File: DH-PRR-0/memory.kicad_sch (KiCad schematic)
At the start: 7 parts, among them J2 Micro_SD_Card_Det2, J3 USB3_A

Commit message: alternate power topologies
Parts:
- renumbered R16 to R30, R17 to R31, R18 to R32, R19 to R33, R20 to R34
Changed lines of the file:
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@@
 		(dnp no)
 		(fields_autoplaced yes)
-		(property "Reference" "#PWR034"
+		(property "Reference" "#PWR056"
 			(at 152.4 107.95 0)
 			(hide yes)
@@
 			(project "DH-PRR-0"
 				(path "/ef4cbb1a-0736-46e9-bda5-652f30ffa2fe/64c9e3bf-941e-41e6-9266-e7d08c7e7040"
-					(reference "#PWR034")
+					(reference "#PWR056")
 					(unit 1)
 				)
@@
 		(dnp no)
 		(fields_autoplaced yes)
-		(property "Reference" "#PWR033"
+		(property "Reference" "#PWR057"
 			(at 165.1 154.94 0)
 			(hide yes)
@@
 			(project "DH-PRR-0"
 				(path "/ef4cbb1a-0736-46e9-bda5-652f30ffa2fe/64c9e3bf-941e-41e6-9266-e7d08c7e7040"
-					(reference "#PWR033")
+					(reference "#PWR057")
 					(unit 1)
 				)
@@
 		(in_pos_files yes)
 		(dnp no)
-		(property "Reference" "R19"
+		(property "Reference" "R33"
 			(at 163.83 113.03 90)
 			(show_name no)
@@
 			(project "DH-PRR-0"
 				(path "/ef4cbb1a-0736-46e9-bda5-652f30ffa2fe/64c9e3bf-941e-41e6-9266-e7d08c7e7040"
-					(reference "R19")
+					(reference "R33")
 					(unit 1)
 				)
@@
 		(dnp no)
 		(fields_autoplaced yes)
-		(property "Reference" "#PWR036"
+		(property "Reference" "#PWR060"
 			(at 248.92 154.94 0)
 			(hide yes)
@@
 			(project "DH-PRR-0"
 				(path "/ef4cbb1a-0736-46e9-bda5-652f30ffa2fe/64c9e3bf-941e-41e6-9266-e7d08c7e7040"
-					(reference "#PWR036")
+					(reference "#PWR060")
 					(unit 1)
 				)
@@
 		(dnp no)
 		(fields_autoplaced yes)
-		(property "Reference" "#PWR032"
+		(property "Reference" "#PWR059"
 			(at 210.82 154.94 0)
 			(hide yes)
@@
 			(project "DH-PRR-0"
 				(path "/ef4cbb1a-0736-46e9-bda5-652f30ffa2fe/64c9e3bf-941e-41e6-9266-e7d08c7e7040"
-					(reference "#PWR032")
+					(reference "#PWR059")
 					(unit 1)
 				)
@@
 		(in_pos_files yes)
 		(dnp no)
-		(property "Reference" "R20"
+		(property "Reference" "R34"
 			(at 166.37 113.03 90)
 			(show_name no)
@@
 			(project "DH-PRR-0"
 				(path "/ef4cbb1a-0736-46e9-bda5-652f30ffa2fe/64c9e3bf-941e-41e6-9266-e7d08c7e7040"
-					(reference "R20")
+					(reference "R34")
 					(unit 1)
 				)
@@
 		(in_pos_files yes)
 		(dnp no)
-		(property "Reference" "R18"
+		(property "Reference" "R32"
 			(at 161.29 113.03 90)
 			(show_name no)
@@
 			(project "DH-PRR-0"
 				(path "/ef4cbb1a-0736-46e9-bda5-652f30ffa2fe/64c9e3bf-941e-41e6-9266-e7d08c7e7040"
-					(reference "R18")
+					(reference "R32")
 					(unit 1)
 				)
@@
 		(in_pos_files yes)
 		(dnp no)
-		(property "Reference" "R17"
+		(property "Reference" "R31"
 			(at 158.75 113.03 90)
 			(show_name no)
@@
 			(project "DH-PRR-0"
 				(path "/ef4cbb1a-0736-46e9-bda5-652f30ffa2fe/64c9e3bf-941e-41e6-9266-e7d08c7e7040"
-					(reference "R17")
+					(reference "R31")
 					(unit 1)
 				)
@@
 		(in_pos_files yes)
 		(dnp no)
-		(property "Reference" "R16"
+		(property "Reference" "R30"
 			(at 156.21 113.03 90)
 			(show_name no)
@@
 			(project "DH-PRR-0"
 				(path "/ef4cbb1a-0736-46e9-bda5-652f30ffa2fe/64c9e3bf-941e-41e6-9266-e7d08c7e7040"
-					(reference "R16")
+					(reference "R30")
 					(unit 1)
 				)
@@
 		(dnp no)
 		(fields_autoplaced yes)
-		(property "Reference" "#PWR035"
+		(property "Reference" "#PWR058"
 			(at 177.8 154.94 0)
 			(hide yes)
@@
 			(project "DH-PRR-0"
 				(path "/ef4cbb1a-0736-46e9-bda5-652f30ffa2fe/64c9e3bf-941e-41e6-9266-e7d08c7e7040"
-					(reference "#PWR035")
-					(unit 1)
-				)
+					(reference "#PWR058")
+					(unit 1)
+				)

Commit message: mcu bootmode
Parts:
- renumbered R30 to R13, R31 to R14, R32 to R15, R33 to R16, R34 to R17
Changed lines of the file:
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@@
 		(dnp no)
 		(fields_autoplaced yes)
-		(property "Reference" "#PWR056"
+		(property "Reference" "#PWR042"
 			(at 152.4 107.95 0)
 			(hide yes)
@@
 			(project "DH-PRR-0"
 				(path "/ef4cbb1a-0736-46e9-bda5-652f30ffa2fe/64c9e3bf-941e-41e6-9266-e7d08c7e7040"
-					(reference "#PWR056")
+					(reference "#PWR042")
 					(unit 1)
 				)
@@
 		(dnp no)
 		(fields_autoplaced yes)
-		(property "Reference" "#PWR057"
+		(property "Reference" "#PWR043"
 			(at 165.1 154.94 0)
 			(hide yes)
@@
 			(project "DH-PRR-0"
 				(path "/ef4cbb1a-0736-46e9-bda5-652f30ffa2fe/64c9e3bf-941e-41e6-9266-e7d08c7e7040"
-					(reference "#PWR057")
+					(reference "#PWR043")
 					(unit 1)
 				)
@@
 		(in_pos_files yes)
 		(dnp no)
-		(property "Reference" "R33"
+		(property "Reference" "R16"
 			(at 163.83 113.03 90)
 			(show_name no)
@@
 			(project "DH-PRR-0"
 				(path "/ef4cbb1a-0736-46e9-bda5-652f30ffa2fe/64c9e3bf-941e-41e6-9266-e7d08c7e7040"
-					(reference "R33")
+					(reference "R16")
 					(unit 1)
 				)
@@
 		(dnp no)
 		(fields_autoplaced yes)
-		(property "Reference" "#PWR060"
+		(property "Reference" "#PWR046"
 			(at 248.92 154.94 0)
 			(hide yes)
@@
 			(project "DH-PRR-0"
 				(path "/ef4cbb1a-0736-46e9-bda5-652f30ffa2fe/64c9e3bf-941e-41e6-9266-e7d08c7e7040"
-					(reference "#PWR060")
+					(reference "#PWR046")
 					(unit 1)
 				)
@@
 		(dnp no)
 		(fields_autoplaced yes)
-		(property "Reference" "#PWR059"
+		(property "Reference" "#PWR045"
 			(at 210.82 154.94 0)
 			(hide yes)
@@
 			(project "DH-PRR-0"
 				(path "/ef4cbb1a-0736-46e9-bda5-652f30ffa2fe/64c9e3bf-941e-41e6-9266-e7d08c7e7040"
-					(reference "#PWR059")
+					(reference "#PWR045")
 					(unit 1)
 				)
@@
 		(in_pos_files yes)
 		(dnp no)
-		(property "Reference" "R34"
+		(property "Reference" "R17"
 			(at 166.37 113.03 90)
 			(show_name no)
@@
 			(project "DH-PRR-0"
 				(path "/ef4cbb1a-0736-46e9-bda5-652f30ffa2fe/64c9e3bf-941e-41e6-9266-e7d08c7e7040"
-					(reference "R34")
+					(reference "R17")
 					(unit 1)
 				)
@@
 		(in_pos_files yes)
 		(dnp no)
-		(property "Reference" "R32"
+		(property "Reference" "R15"
 			(at 161.29 113.03 90)
 			(show_name no)
@@
 			(project "DH-PRR-0"
 				(path "/ef4cbb1a-0736-46e9-bda5-652f30ffa2fe/64c9e3bf-941e-41e6-9266-e7d08c7e7040"
-					(reference "R32")
+					(reference "R15")
 					(unit 1)
 				)
@@
 		(in_pos_files yes)
 		(dnp no)
-		(property "Reference" "R31"
+		(property "Reference" "R14"
 			(at 158.75 113.03 90)
 			(show_name no)
@@
 			(project "DH-PRR-0"
 				(path "/ef4cbb1a-0736-46e9-bda5-652f30ffa2fe/64c9e3bf-941e-41e6-9266-e7d08c7e7040"
-					(reference "R31")
+					(reference "R14")
 					(unit 1)
 				)
@@
 		(in_pos_files yes)
 		(dnp no)
-		(property "Reference" "R30"
+		(property "Reference" "R13"
 			(at 156.21 113.03 90)
 			(show_name no)
@@
 			(project "DH-PRR-0"
 				(path "/ef4cbb1a-0736-46e9-bda5-652f30ffa2fe/64c9e3bf-941e-41e6-9266-e7d08c7e7040"
-					(reference "R30")
+					(reference "R13")
 					(unit 1)
 				)
@@
 		(dnp no)
 		(fields_autoplaced yes)
-		(property "Reference" "#PWR058"
+		(property "Reference" "#PWR044"
 			(at 177.8 154.94 0)
 			(hide yes)
@@
 			(project "DH-PRR-0"
 				(path "/ef4cbb1a-0736-46e9-bda5-652f30ffa2fe/64c9e3bf-941e-41e6-9266-e7d08c7e7040"
-					(reference "#PWR058")
-					(unit 1)
-				)
+					(reference "#PWR044")
+					(unit 1)
+				)

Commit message: i dont remember
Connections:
- net +5V: now reaches J3.1 (VBUS)
- net DUSB-: now reaches J3.2 (D-)
- net DUSB+: now reaches J3.3 (D+)
- no-connect marks 0 -> 4
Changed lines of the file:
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@@
 		(color 0 0 0 0)
 	)
+	(no_connect
+		(at 266.7 137.16)
+	)
+	(no_connect
+		(at 266.7 139.7)
+	)
+	(no_connect
+		(at 266.7 129.54)
+	)
+	(no_connect
+		(at 266.7 132.08)
+	)
 	(wire
 		(pts
@@
 	(wire
 		(pts
+			(xy 267.97 115.57) (xy 267.97 116.84)
+		)
+		(stroke
+			(width 0)
+			(type default)
+		)
+	)
+	(wire
+		(pts
 			(xy 177.8 147.32) (xy 177.8 148.59)
 		)
@@
 	(wire
 		(pts
+			(xy 266.7 124.46) (xy 267.97 124.46)
+		)
+		(stroke
+			(width 0)
+			(type default)
+		)
+	)
+	(wire
+		(pts
 			(xy 152.4 118.11) (xy 154.94 118.11)
 		)
@@
 	(wire
 		(pts
+			(xy 266.7 116.84) (xy 267.97 116.84)
+		)
+		(stroke
+			(width 0)
+			(type default)
+		)
+	)
+	(wire
+		(pts
+			(xy 266.7 121.92) (xy 267.97 121.92)
+		)
+		(stroke
+			(width 0)
+			(type default)
+		)
+	)
+	(wire
+		(pts
 			(xy 254 144.78) (xy 254 146.05)
 		)
@@
 		)
 	)
+	(hierarchical_label "DUSB+"
+		(shape input)
+		(at 267.97 124.46 0)
+		(effects
+			(font
+				(size 1.27 1.27)
+			)
+			(justify left)
+		)
+	)
 	(hierarchical_label "D0"
 		(shape input)
@@
 			)
 			(justify right)
+		)
+	)
+	(hierarchical_label "DUSB-"
+		(shape input)
+		(at 267.97 121.92 0)
+		(effects
+			(font
+				(size 1.27 1.27)
+			)
+			(justify left)
 		)
 	)
@@
 					(unit 1)
 				)
+			)
+		)
+	)
+	(symbol
+		(lib_id "power:+5V")
+		(at 267.97 115.57 0)
+		(unit 1)
+		(body_style 1)
+		(exclude_from_sim no)
+		(in_bom yes)
+		(on_board yes)
+		(in_pos_files yes)
+		(dnp no)
+		(fields_autoplaced yes)
+		(property "Reference" "#PWR049"
+			(at 267.97 119.38 0)
+			(hide yes)
+			(show_name no)
+			(do_not_autoplace no)
+			(effects
+				(font
+					(size 1.27 1.27)
+				)
+			)
+		)
+		(property "Value" "+5V"
+			(at 267.97 110.49 0)
+			(show_name no)
+			(do_not_autoplace no)
+			(effects
+				(font
+					(size 1.27 1.27)
+				)
+			)
+		)
+		(property "Footprint" ""
+			(at 267.97 115.57 0)
+			(hide yes)
+			(show_name no)
+			(do_not_autoplace no)
+			(effects
+				(font
+					(size 1.27 1.27)
+				)
+			)
+		)
+		(property "Datasheet" ""
+			(at 267.97 115.57 0)
+			(hide yes)
+			(show_name no)
+			(do_not_autoplace no)
+			(effects
+				(font
+					(size 1.27 1.27)
+				)
+			)
+		)
+		(property "Description" "Power symbol creates a global label with name \"+5V\""
+			(at 267.97 115.57 0)
+			(hide yes)
+			(show_name no)
+			(do_not_autoplace no)
+			(effects
+				(font
+					(size 1.27 1.27)
+				)
+			)
+		)
+		(pin "1"
+		)
+		(instances
+			(project "DH-PRR-0"
+				(path "/ef4cbb1a-0736-46e9-bda5-652f30ffa2fe/64c9e3bf-941e-41e6-9266-e7d08c7e7040"
+					(reference "#PWR049")
+					(unit 1)
+				)

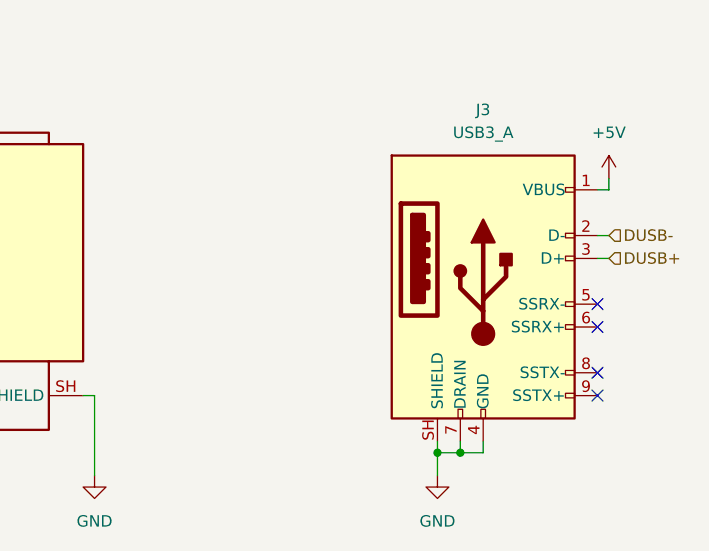
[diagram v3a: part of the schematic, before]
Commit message: uart IC to use USB interface for memory instead
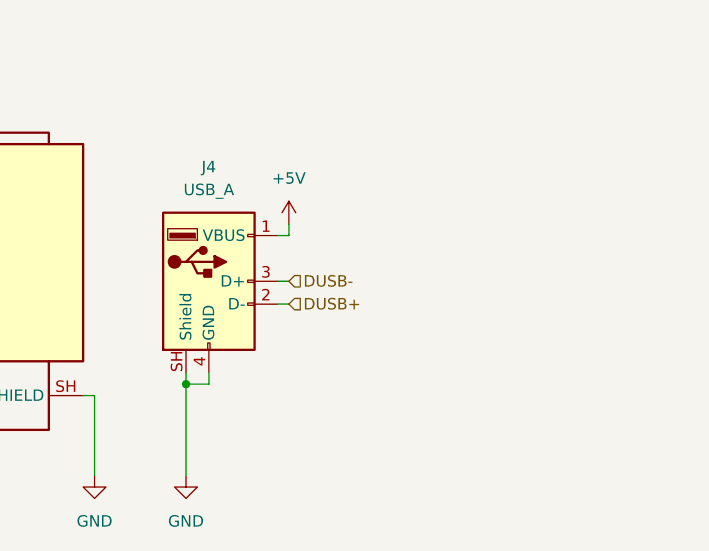
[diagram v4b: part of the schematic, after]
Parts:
- removed J3: USB3_A, symbol Connector:USB3_A
- added J4: USB_A, symbol Connector:USB_A
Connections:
- net +5V: now also J4.1 (VBUS)
- net DUSB+: now also J4.2 (D-)
- net DUSB-: now also J4.3 (D+)
- net GND: now also J4.4 (GND), J4.SH (Shield)
- no-connect marks 4 -> 0
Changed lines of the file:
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@@
-	)
-	(junction
-		(at 251.46 146.05)
-		(diameter 0)
-		(color 0 0 0 0)
 	)
 	(junction
@@
 	)
 	(junction
-		(at 248.92 146.05)
+		(at 220.98 138.43)
 		(diameter 0)
 		(color 0 0 0 0)
@@
 		(color 0 0 0 0)
 	)
-	(no_connect
-		(at 266.7 137.16)
-	)
-	(no_connect
-		(at 266.7 139.7)
-	)
-	(no_connect
-		(at 266.7 129.54)
-	)
-	(no_connect
-		(at 266.7 132.08)
-	)
 	(wire
 		(pts
@@
 	(wire
 		(pts
-			(xy 251.46 146.05) (xy 254 146.05)
-		)
-		(stroke
-			(width 0)
-			(type default)
-		)
-	)
-	(wire
-		(pts
 			(xy 210.82 139.7) (xy 210.82 148.59)
 		)
@@
 	(wire
 		(pts
-			(xy 251.46 144.78) (xy 251.46 146.05)
+			(xy 223.52 137.16) (xy 223.52 138.43)
 		)
 		(stroke
@@
 	(wire
 		(pts
-			(xy 248.92 146.05) (xy 248.92 148.59)
+			(xy 220.98 138.43) (xy 220.98 148.59)
 		)
 		(stroke
@@
 	(wire
 		(pts
-			(xy 267.97 115.57) (xy 267.97 116.84)
+			(xy 232.41 120.65) (xy 232.41 121.92)
 		)
 		(stroke
@@
 	(wire
 		(pts
-			(xy 248.92 146.05) (xy 251.46 146.05)
+			(xy 220.98 138.43) (xy 223.52 138.43)
 		)
 		(stroke
@@
 	(wire
 		(pts
-			(xy 266.7 124.46) (xy 267.97 124.46)
+			(xy 231.14 129.54) (xy 232.41 129.54)
 		)
 		(stroke
@@
 	(wire
 		(pts
-			(xy 248.92 144.78) (xy 248.92 146.05)
-		)
-		(stroke
-			(width 0)
-			(type default)
-		)
-	)
-	(wire
-		(pts
-			(xy 266.7 116.84) (xy 267.97 116.84)
-		)
-		(stroke
-			(width 0)
-			(type default)
-		)
-	)
-	(wire
-		(pts
-			(xy 266.7 121.92) (xy 267.97 121.92)
-		)
-		(stroke
-			(width 0)
-			(type default)
-		)
-	)
-	(wire
-		(pts
-			(xy 254 144.78) (xy 254 146.05)
+			(xy 220.98 137.16) (xy 220.98 138.43)
+		)
+		(stroke
+			(width 0)
+			(type default)
+		)
+	)
+	(wire
+		(pts
+			(xy 231.14 121.92) (xy 232.41 121.92)
+		)
+		(stroke
+			(width 0)
+			(type default)
+		)
+	)
+	(wire
+		(pts
+			(xy 231.14 127) (xy 232.41 127)
 		)
 		(stroke
@@
 	(hierarchical_label "DUSB+"
 		(shape input)
-		(at 267.97 124.46 0)
+		(at 232.41 129.54 0)
 		(effects
 			(font
@@
 	(hierarchical_label "DUSB-"
 		(shape input)
-		(at 267.97 121.92 0)
+		(at 232.41 127 0)
 		(effects
 			(font
@@
 	)
 	(symbol
+		(lib_id "Connector:USB_A")
+		(at 223.52 127 0)
+		(unit 1)
+		(body_style 1)
+		(exclude_from_sim no)
+		(in_bom yes)
+		(on_board yes)
+		(in_pos_files yes)
+		(dnp no)
+		(fields_autoplaced yes)
+		(property "Reference" "J4"
+			(at 223.52 114.3 0)
+			(show_name no)
+			(do_not_autoplace no)
+			(effects
+				(font
+					(size 1.27 1.27)
+				)
+			)
+		)
+		(property "Value" "USB_A"
+			(at 223.52 116.84 0)
+			(show_name no)
+			(do_not_autoplace no)
+			(effects
+				(font
+					(size 1.27 1.27)
+				)
+			)
+		)
+		(property "Footprint" ""
+			(at 227.33 128.27 0)
+			(hide yes)
+			(show_name no)
+			(do_not_autoplace no)
+			(effects
+				(font
+					(size 1.27 1.27)
+				)
+			)
+		)
+		(property "Datasheet" ""
+			(at 227.33 128.27 0)
+			(hide yes)
+			(show_name no)
+			(do_not_autoplace no)
+			(effects
+				(font
+					(size 1.27 1.27)
+				)
+			)
+		)
+		(property "Description" "USB Type A connector"
+			(at 223.52 127 0)
+			(hide yes)
+			(show_name no)
+			(do_not_autoplace no)
+			(effects
+				(font
+					(size 1.27 1.27)
+				)
+			)
+		)
+		(pin "2"
+		)
+		(pin "4"
+		)
+		(pin "3"
+		)
+		(pin "SH"
+		)
+		(pin "1"
+		)
+		(instances
+			(project "DH-PRR-0"
+				(path "/ef4cbb1a-0736-46e9-bda5-652f30ffa2fe/64c9e3bf-941e-41e6-9266-e7d08c7e7040"
+					(reference "J4")
+					(unit 1)
+				)
+			)
+		)
+	)
+	(symbol
 		(lib_id "power:GND")
 		(at 165.1 148.59 0)
@@
 	(symbol
 		(lib_id "power:+5V")
-		(at 267.97 115.57 0)
+		(at 232.41 120.65 0)
 		(unit 1)
 		(body_style 1)
@@
 		(fields_autoplaced yes)
 		(property "Reference" "#PWR049"
-			(at 267.97 119.38 0)
+			(at 232.41 124.46 0)
 			(hide yes)
 			(show_name no)
@@
 		)
 		(property "Value" "+5V"
-			(at 267.97 110.49 0)
+			(at 232.41 115.57 0)
 			(show_name no)
 			(do_not_autoplace no)
@@
 		)
 		(property "Footprint" ""
-			(at 267.97 115.57 0)
+			(at 232.41 120.65 0)
 			(hide yes)
 			(show_name no)
@@
 		)
 		(property "Datasheet" ""
-			(at 267.97 115.57 0)
+			(at 232.41 120.65 0)
 			(hide yes)
 			(show_name no)
@@
 		)
 		(property "Description" "Power symbol creates a global label with name \"+5V\""
-			(at 267.97 115.57 0)
+			(at 232.41 120.65 0)
 			(hide yes)
 			(show_name no)
@@
 	(symbol
 		(lib_id "power:GND")
-		(at 248.92 148.59 0)
+		(at 220.98 148.59 0)
 		(unit 1)
 		(body_style 1)
@@
 		(fields_autoplaced yes)
 		(property "Reference" "#PWR046"
-			(at 248.92 154.94 0)
+			(at 220.98 154.94 0)
 			(hide yes)
 			(show_name no)
@@
 		)
 		(property "Value" "GND"
-			(at 248.92 153.67 0)
+			(at 220.98 153.67 0)
 			(show_name no)
 			(do_not_autoplace no)
@@
 		)
 		(property "Footprint" ""
-			(at 248.92 148.59 0)
+			(at 220.98 148.59 0)
 			(hide yes)
 			(show_name no)
@@
 		)
 		(property "Datasheet" ""
-			(at 248.92 148.59 0)
+			(at 220.98 148.59 0)
 			(hide yes)
 			(show_name no)
@@
 		)
 		(property "Description" "Power symbol creates a global label with name \"GND\" , ground"
-			(at 248.92 148.59 0)
+			(at 220.98 148.59 0)
 			(hide yes)
 			(show_name no)
@@
 					(unit 1)
 				)
-			)
-		)
-	)
-	(symbol
-		(lib_id "Connector:USB3_A")
-		(at 254 127 0)
-		(unit 1)
-		(body_style 1)
-		(exclude_from_sim no)
-		(in_bom yes)
-		(on_board yes)
-		(in_pos_files yes)
-		(dnp no)
-		(fields_autoplaced yes)
-		(property "Reference" "J3"
-			(at 254 107.95 0)
-			(show_name no)
-			(do_not_autoplace no)
-			(effects
-				(font
-					(size 1.27 1.27)
-				)
-			)
-		)
-		(property "Value" "USB3_A"
-			(at 254 110.49 0)
-			(show_name no)
-			(do_not_autoplace no)
-			(effects
-				(font
-					(size 1.27 1.27)
-				)
-			)
-		)
-		(property "Footprint" ""
-			(at 257.81 124.46 0)
-			(hide yes)
-			(show_name no)
-			(do_not_autoplace no)
-			(effects
-				(font
-					(size 1.27 1.27)
-				)
-			)
-		)
-		(property "Datasheet" ""
-			(at 257.81 124.46 0)
-			(hide yes)
-			(show_name no)
-			(do_not_autoplace no)
-			(effects
-				(font
-					(size 1.27 1.27)
-				)
-			)
-		)
-		(property "Description" "USB 3.0 A connector"
-			(at 254 127 0)
-			(hide yes)
-			(show_name no)
-			(do_not_autoplace no)
-			(effects
-				(font
-					(size 1.27 1.27)
-				)
-			)
-		)
-		(pin "5"
-		)
-		(pin "9"
-		)
-		(pin "1"
-		)
-		(pin "3"
-		)
-		(pin "2"
-		)
-		(pin "7"
-		)
-		(pin "4"
-		)
-		(pin "6"
-		)
-		(pin "SH"
-		)
-		(pin "8"
-		)
-		(instances
-			(project "DH-PRR-0"
-				(path "/ef4cbb1a-0736-46e9-bda5-652f30ffa2fe/64c9e3bf-941e-41e6-9266-e7d08c7e7040"
-					(reference "J3")
-					(unit 1)
-				)

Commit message: added usb to spi to free up USB bus
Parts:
- added U8: MCP2210x-MQ, Package_DFN_QFN:QFN-20-1EP_5x5mm_P0.65mm_EP3.35x3.35mm, symbol Interface_USB:MCP2210x-MQ
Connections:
- net DUSB+: no longer names the net of J4.2 (D-)
- net DUSB+: now also U8.15 (D-)
- net DUSB-: no longer names the net of J4.3 (D+)
- net DUSB-: now also U8.16 (D+)
- new net ~{RST}: U8.1 (~{RST})
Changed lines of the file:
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@@
+	(wire
+		(pts
+			(xy 238.76 116.84) (xy 238.76 127)
+		)
+		(stroke
+			(width 0)
+			(type default)
+		)
+	)
 	(wire
 		(pts
@@
 	(wire
 		(pts
+			(xy 238.76 116.84) (xy 243.84 116.84)
+		)
+		(stroke
+			(width 0)
+			(type default)
+		)
+	)
+	(wire
+		(pts
 			(xy 232.41 120.65) (xy 232.41 121.92)
 		)
@@
 	(wire
 		(pts
+			(xy 241.3 119.38) (xy 243.84 119.38)
+		)
+		(stroke
+			(width 0)
+			(type default)
+		)
+	)
+	(wire
+		(pts
 			(xy 162.56 105.41) (xy 162.56 106.68)
 		)
@@
 	(wire
 		(pts
+			(xy 242.57 111.76) (xy 243.84 111.76)
+		)
+		(stroke
+			(width 0)
+			(type default)
+		)
+	)
+	(wire
+		(pts
 			(xy 165.1 105.41) (xy 165.1 106.68)
 		)
@@
 	(wire
 		(pts
-			(xy 231.14 129.54) (xy 232.41 129.54)
+			(xy 231.14 129.54) (xy 241.3 129.54)
 		)
 		(stroke
@@
 	(wire
 		(pts
+			(xy 241.3 119.38) (xy 241.3 129.54)
+		)
+		(stroke
+			(width 0)
+			(type default)
+		)
+	)
+	(wire
+		(pts
 			(xy 231.14 121.92) (xy 232.41 121.92)
 		)
@@
 	(wire
 		(pts
-			(xy 231.14 127) (xy 232.41 127)
+			(xy 231.14 127) (xy 238.76 127)
 		)
 		(stroke
@@
 		)
 	)
-	(hierarchical_label "DUSB+"
-		(shape input)
-		(at 232.41 129.54 0)
-		(effects
-			(font
-				(size 1.27 1.27)
-			)
-			(justify left)
-		)
-	)
 	(hierarchical_label "D0"
 		(shape input)
@@
 		)
 	)
-	(hierarchical_label "DUSB-"
-		(shape input)
-		(at 232.41 127 0)
-		(effects
-			(font
-				(size 1.27 1.27)
-			)
-			(justify left)
-		)
-	)
 	(hierarchical_label "D2"
 		(shape input)
@@
 		(shape input)
 		(at 152.4 123.19 180)
+		(effects
+			(font
+				(size 1.27 1.27)
+			)
+			(justify right)
+		)
+	)
+	(hierarchical_label "~{RST}"
+		(shape input)
+		(at 242.57 111.76 180)
 		(effects
 			(font
@@
 					(unit 1)
 				)
+			)
+		)
+	)
+	(symbol
+		(lib_id "Interface_USB:MCP2210x-MQ")
+		(at 256.54 127 0)
+		(unit 1)
+		(body_style 1)
+		(exclude_from_sim no)
+		(in_bom yes)
+		(on_board yes)
+		(in_pos_files yes)
+		(dnp no)
+		(fields_autoplaced yes)
+		(property "Reference" "U8"
+			(at 258.6833 104.14 0)
+			(show_name no)
+			(do_not_autoplace no)
+			(effects
+				(font
+					(size 1.27 1.27)
+				)
+				(justify left)
+			)
+		)
+		(property "Value" "MCP2210x-MQ"
+			(at 258.6833 106.68 0)
+			(show_name no)
+			(do_not_autoplace no)
+			(effects
+				(font
+					(size 1.27 1.27)
+				)
+				(justify left)
+			)
+		)
+		(property "Footprint" "Package_DFN_QFN:QFN-20-1EP_5x5mm_P0.65mm_EP3.35x3.35mm"
+			(at 256.54 101.6 0)
+			(hide yes)
+			(show_name no)
+			(do_not_autoplace no)
+			(effects
+				(font
+					(size 1.27 1.27)
+				)
+			)
+		)
+		(property "Datasheet" "https://ww1.microchip.com/downloads/en/DeviceDoc/22288A.pdf"
+			(at 254 106.68 0)
+			(hide yes)
+			(show_name no)
+			(do_not_autoplace no)
+			(effects
+				(font
+					(size 1.27 1.27)
+				)
+			)
+		)
+		(property "Description" "USB to SPI Protocol Converter with GPIO, QFN-20"
+			(at 256.54 127 0)
+			(hide yes)
+			(show_name no)
+			(do_not_autoplace no)
+			(effects
+				(font
+					(size 1.27 1.27)
+				)
+			)
+		)
+		(pin "20"
+		)
+		(pin "17"
+		)
+		(pin "21"
+		)
+		(pin "19"
+		)
+		(pin "10"
+		)
+		(pin "7"
+		)
+		(pin "4"
+		)
+		(pin "18"
+		)
+		(pin "15"
+		)
+		(pin "6"
+		)
+		(pin "8"
+		)
+		(pin "16"
+		)
+		(pin "12"
+		)
+		(pin "14"
+		)
+		(pin "11"
+		)
+		(pin "5"
+		)
+		(pin "1"
+		)
+		(pin "2"
+		)
+		(pin "3"
+		)
+		(pin "9"
+		)
+		(pin "13"
+		)
+		(instances
+			(project "DH-PRR-0"
+				(path "/ef4cbb1a-0736-46e9-bda5-652f30ffa2fe/64c9e3bf-941e-41e6-9266-e7d08c7e7040"
+					(reference "U8")
+					(unit 1)
+				)
